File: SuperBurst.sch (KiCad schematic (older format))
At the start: 8 parts, among them P1 CONN_01X03, P2 CONN_01X03, Q1 Si2301, Q2 Si2301

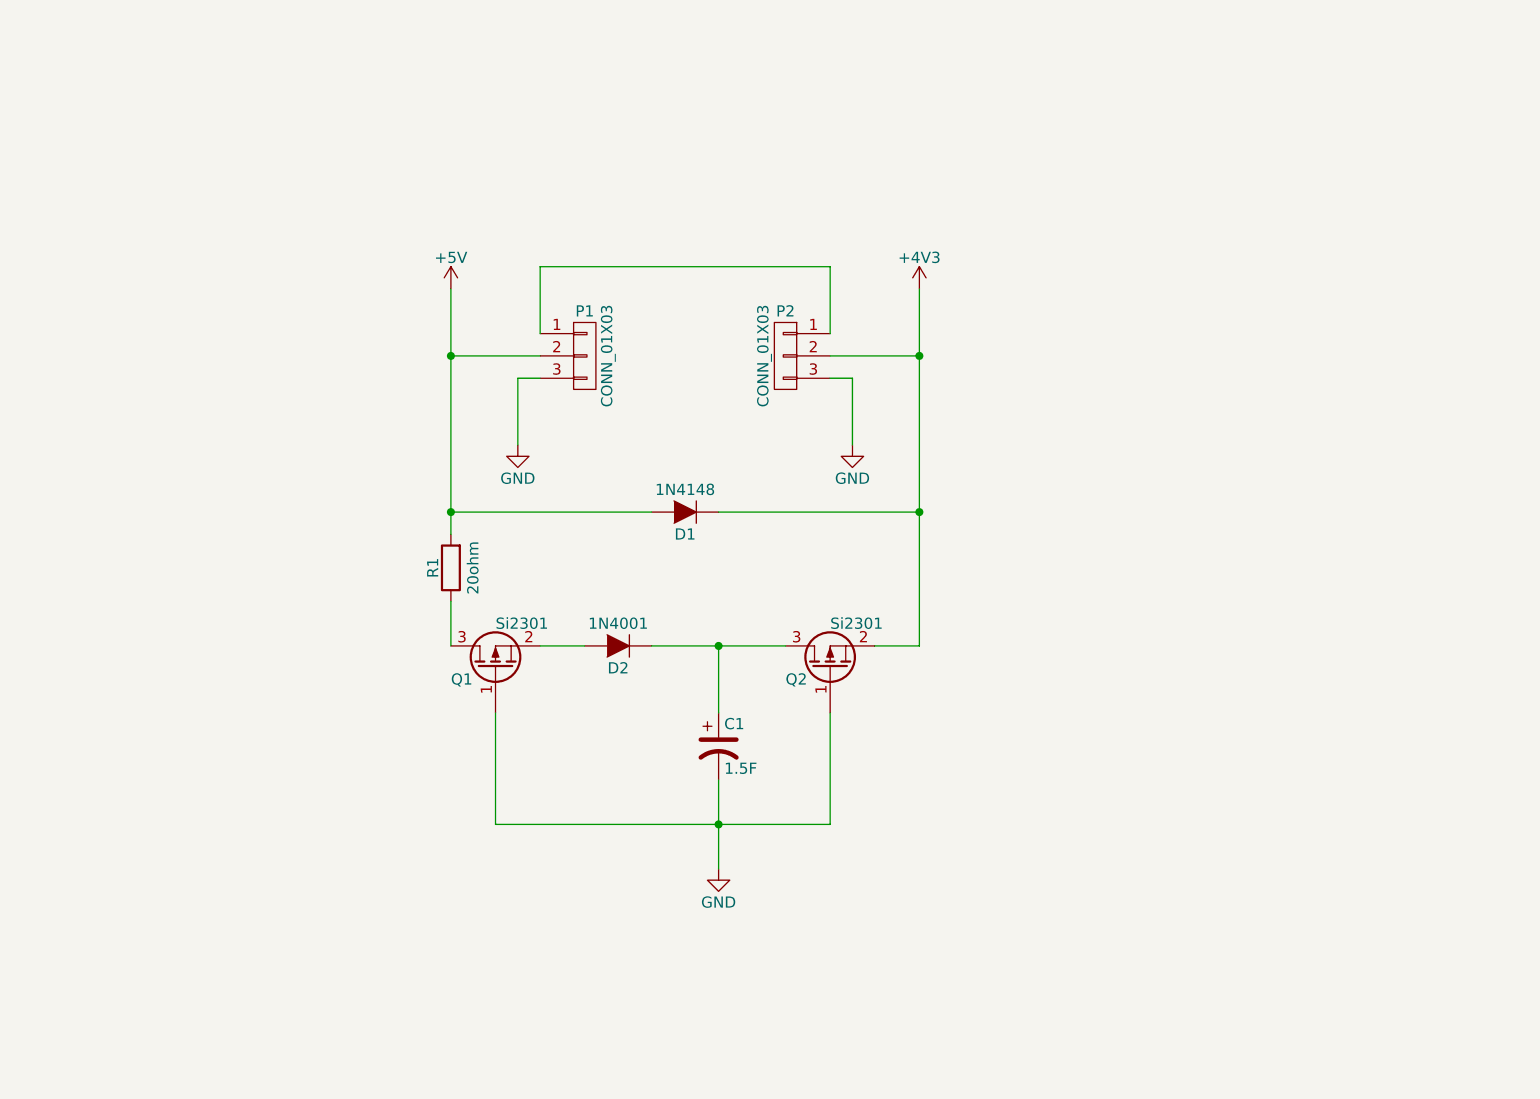
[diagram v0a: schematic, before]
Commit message: Low ESR supercap with voltage detector
Advanced discrete component circuit that charges the supercap, then via
mosfets as switches, exposes the charged supercap to downstream loads.
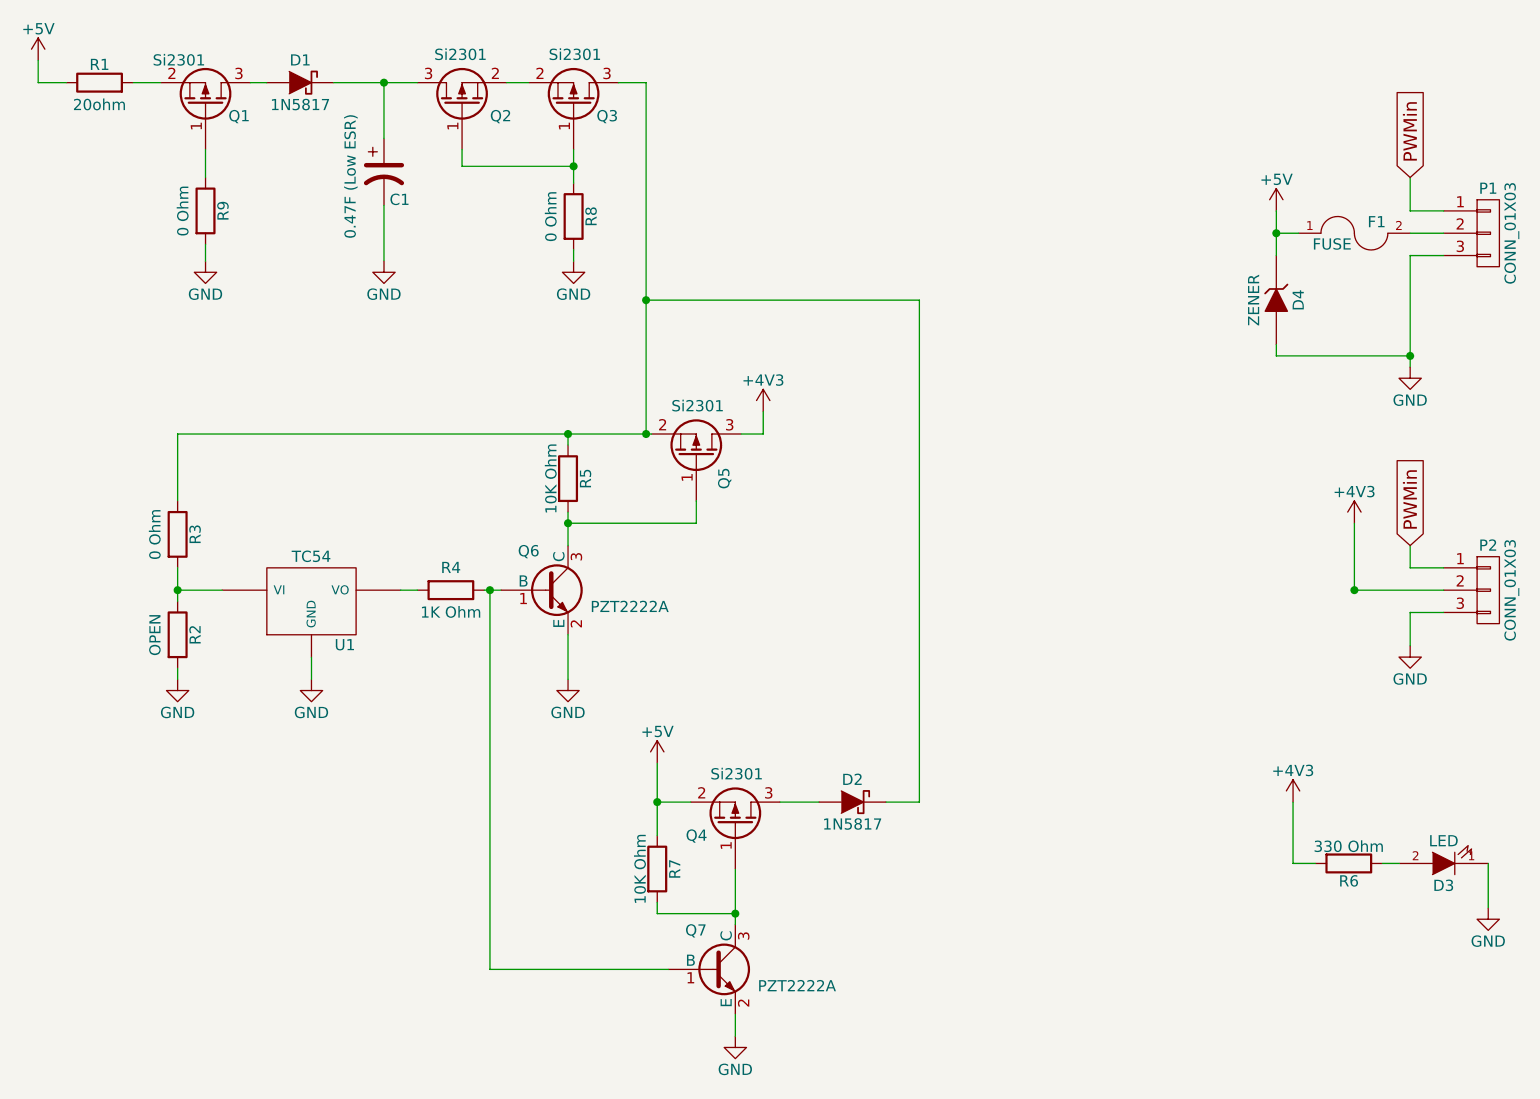
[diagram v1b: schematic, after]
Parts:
- removed D1: 1N4148, Diodes_ThroughHole:Diode_DO-35_SOD27_Horizontal_RM10, symbol D
- removed D2: 1N4001, Diodes_ThroughHole:Diode_DO-35_SOD27_Horizontal_RM10, symbol D
- added D1, D2: 1N5817, Diodes_SMD:SMA-SMB_Universal_Handsoldering, symbol D_Schottky
- added D3: LED, Resistors_SMD:R_0805_HandSoldering, symbol LED
- added D4: ZENER, Diodes_SMD:SMA-SMB_Universal_Handsoldering, symbol ZENER
- added F1: FUSE, Resistors_SMD:R_0805_HandSoldering, symbol FUSE
- added Q3, Q4, Q5: Si2301, TO_SOT_Packages_SMD:SOT-23_Handsoldering, symbol Q_PMOS_GSD
- added Q6, Q7: PZT2222A, TO_SOT_Packages_SMD:SOT-23_Handsoldering, symbol PZT2222A
- added R2: OPEN, Resistors_SMD:R_0805_HandSoldering, symbol R
- added R3, R8, R9: 0 Ohm, Resistors_SMD:R_0805_HandSoldering, symbol R
- added R4: 1K Ohm, Resistors_SMD:R_0805_HandSoldering, symbol R
- added R5, R7: 10K Ohm, Resistors_SMD:R_0805_HandSoldering, symbol R
- added R6: 330 Ohm, Resistors_SMD:R_0805_HandSoldering, symbol R
- added U1: TC54, TO_SOT_Packages_SMD:SOT-23_Handsoldering, symbol TC54
- C1: value 1.5F -> 0.47F (Low ESR)
- Q1, Q2: footprint TO_SOT_Packages_SMD:SOT-23 -> TO_SOT_Packages_SMD:SOT-23_Handsoldering
- R1: footprint Resistors_ThroughHole:Resistor_Horizontal_RM10mm -> Resistors_SMD:R_2512_HandSoldering
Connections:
- net +4V3: now also Q5.3 (D), R6.2; no longer Q2.2 (S)
- net +5V: now also R1.1, D4.1 (K), F1.1, Q4.2 (S), R7.1; no longer P1.2 (P2), R1.2
- net GND: now also D3.1 (K), D4.2 (A), Q6.2 (E), Q7.2 (E), R2.2, R8.2, R9.2, U1.2 (GND); no longer Q1.1 (G), Q2.1 (G)
- net at Q1.2 (S): now also R1.2
- net at Q1.3 (D): now also D1.2 (A); no longer R1.1
- net at C1.1, Q2.3 (D): now also D1.1 (K)
- net PWMin: now reaches P1.1 (P1), P2.1 (P1)
- new net: Q1.1 (G), R9.1
- new net: Q2.1 (G), Q3.1 (G), R8.1
- new net: Q2.2 (S), Q3.2 (S)
- new net: F1.2, P1.2 (P2)
- new net: D2.1 (K), Q3.3 (D), Q5.2 (S), R3.1, R5.1
- new net: Q4.1 (G), Q7.3 (C), R7.2
- new net: D2.2 (A), Q4.3 (D)
- new net: R4.2, U1.1 (VO)
- new net: R2.1, R3.2, U1.3 (VI)
- new net: Q6.1 (B), Q7.1 (B), R4.1
- new net: D3.2 (A), R6.1
- new net: Q5.1 (G), Q6.3 (C), R5.2
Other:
- moved on the sheet: C1, P1, P2, Q1, Q2, R1

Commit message: First Load
Initial load of the board
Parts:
- P2: footprint Pin_Headers:Pin_Header_Angled_1x03 -> SuperCap:Pin_Header_Angled_1x03B
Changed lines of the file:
@@
 F 0 "P2" H 9250 4050 50  0000 C CNN
 F 1 "CONN_01X03" V 9350 3850 50  0000 C CNN
-F 2 "Pin_Headers:Pin_Header_Angled_1x03" H 9250 3850 50  0001 C CNN
+F 2 "SuperCap:Pin_Header_Angled_1x03B" H 9250 3850 50  0001 C CNN
 F 3 "" H 9250 3850 50  0000 C CNN
 	1    9250 3850
